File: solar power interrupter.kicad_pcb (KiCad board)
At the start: 2 copper layers, 25.4 x 33 mm, 18 parts, among them J1 USB_C_Receptacle_USB2.0, J2 Screw_Terminal_01x04, Q1 BSS138, Q2 BSS138, Q3 BSS84

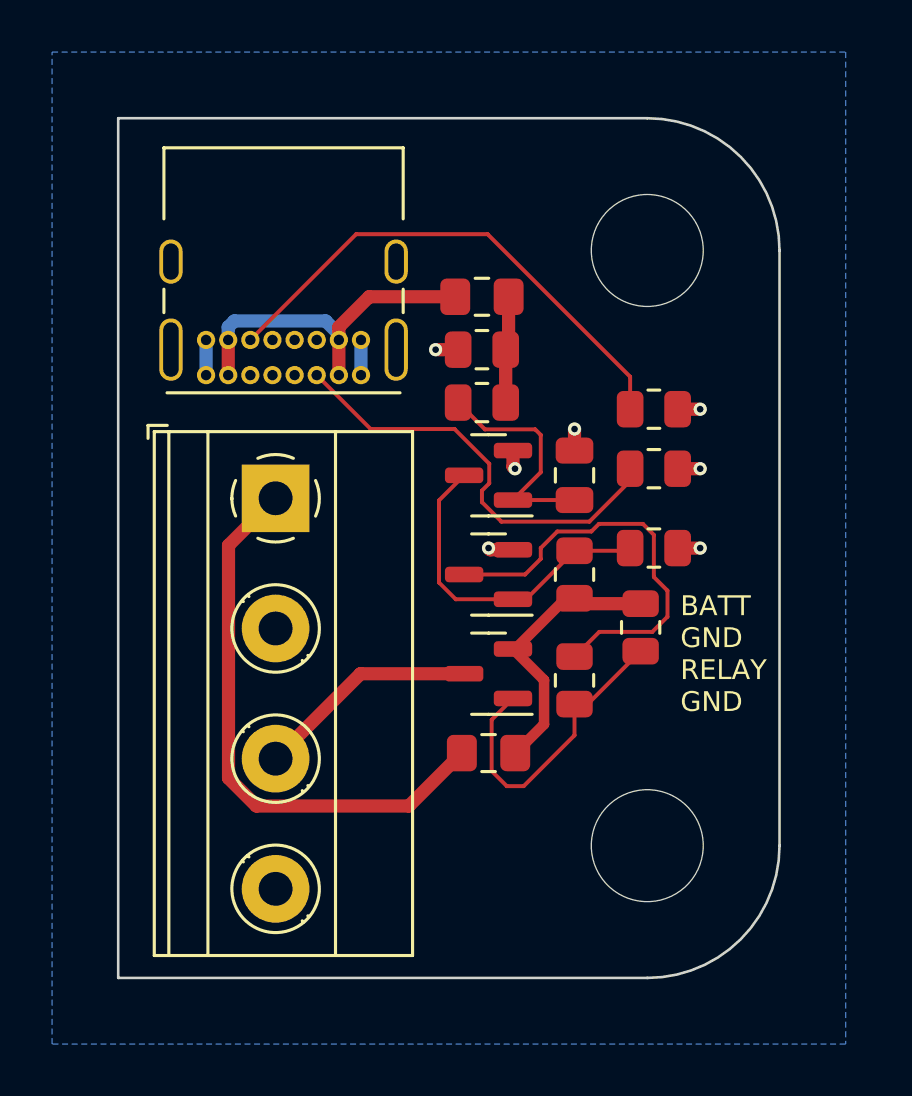
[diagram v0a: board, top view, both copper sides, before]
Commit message: added protection to battery connection, changed pins on connector for safety, added zener diodes to limit Vgs, added protection for relay drive pin
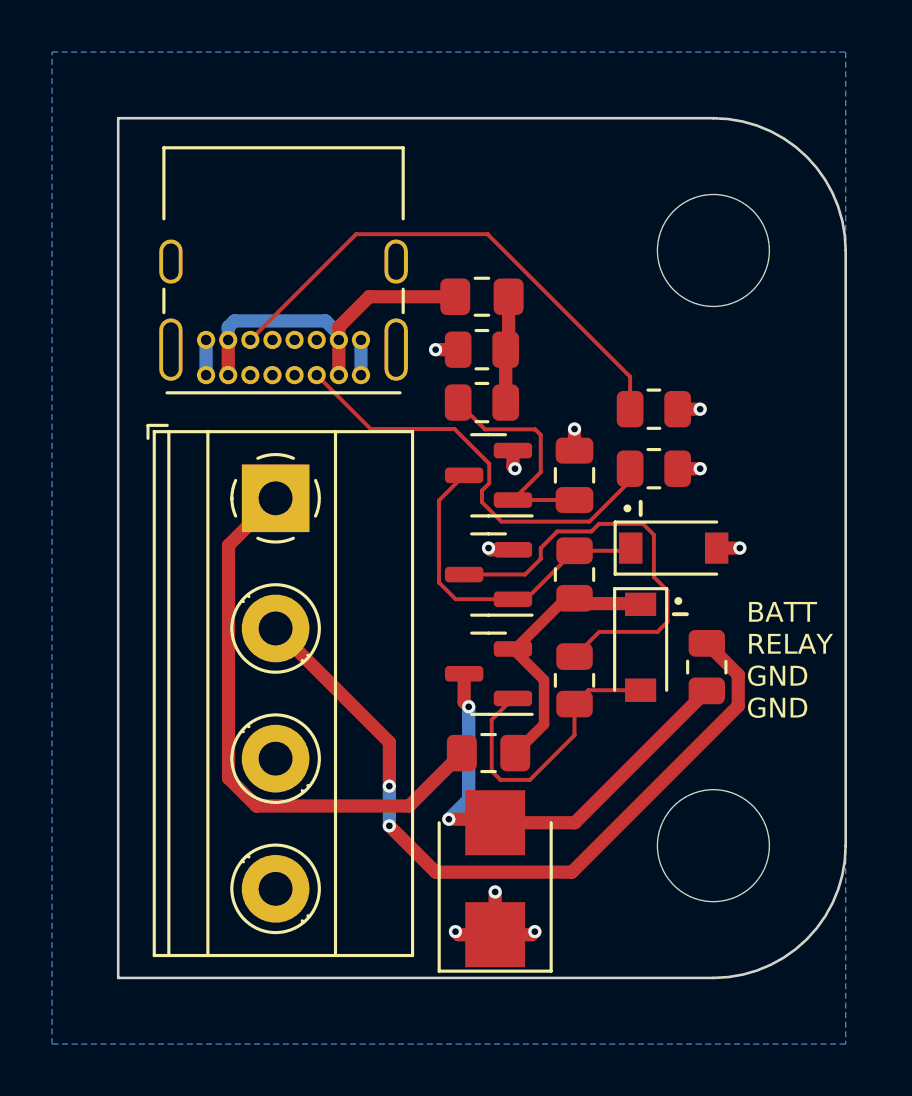
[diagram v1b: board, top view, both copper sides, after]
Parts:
- removed R8: 40K, Resistor_SMD:R_0805_2012Metric
- added D1: D_Zener, Diode_SMD:D_SOD-123, F.Cu at (54.4, 166.4)
- added D2: D_Zener, Diode_SMD:D_SOD-123, F.Cu at (53.1, 170.2)
- added D3: D_TVS, Diode_SMD:D_SMB, F.Cu at (47.5, 179.1)
- F1: value Fuse -> USB Fuse
- F2: value Fuse -> Batt Fuse
- R4, R5: value 60K -> 56k
- R6: value 6K -> 6.2K
- R7: value 40k -> 2.7K
- moved R7 5.00 mm to (55.6, 170.9), turned to 90 degrees
- moved H1 2.54 mm to (55.9, 154.9)
- moved H2 2.54 mm to (55.9, 177.8)
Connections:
- J2 pad 2: GND -> /RELAY
- J2 pad 3: /RELAY -> GND
- Q1 pad 3: Net-(Q1-Pad3) -> Net-(D1-Pad1)
- Q2 pad 1: Net-(Q1-Pad3) -> Net-(D1-Pad1)
- Q3 pad 3: /RELAY -> /RELAY_UNPROTECTED
- R4 pad 2: Net-(Q1-Pad3) -> Net-(D1-Pad1)
- R7 pad 1: Net-(Q1-Pad3) -> /RELAY_UNPROTECTED
- R7 pad 2: GND -> /RELAY
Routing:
- net /RELAY: track 8.59 -> 29.1 mm, vias 0 -> 2
- net /RELAY_UNPROTECTED: track 0.00 -> 18.0 mm, vias 0 -> 2
- net Net-(Q1-Pad3): track 12.3 -> 0.00 mm
- net Net-(D1-Pad1): track 0.00 -> 12.3 mm
- net GND: track 8.68 -> 13.5 mm, vias 7 -> 10
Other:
- board size 25.4 x 33 mm -> 27.9 x 33 mm
- board text added: "BATT RELAY GND GND"
- board text removed: "BATT GND RELAY GND"

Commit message: updated simulation added needed pullup resistor, note this wasn't included in the PCB that I ordered. added images to readme.
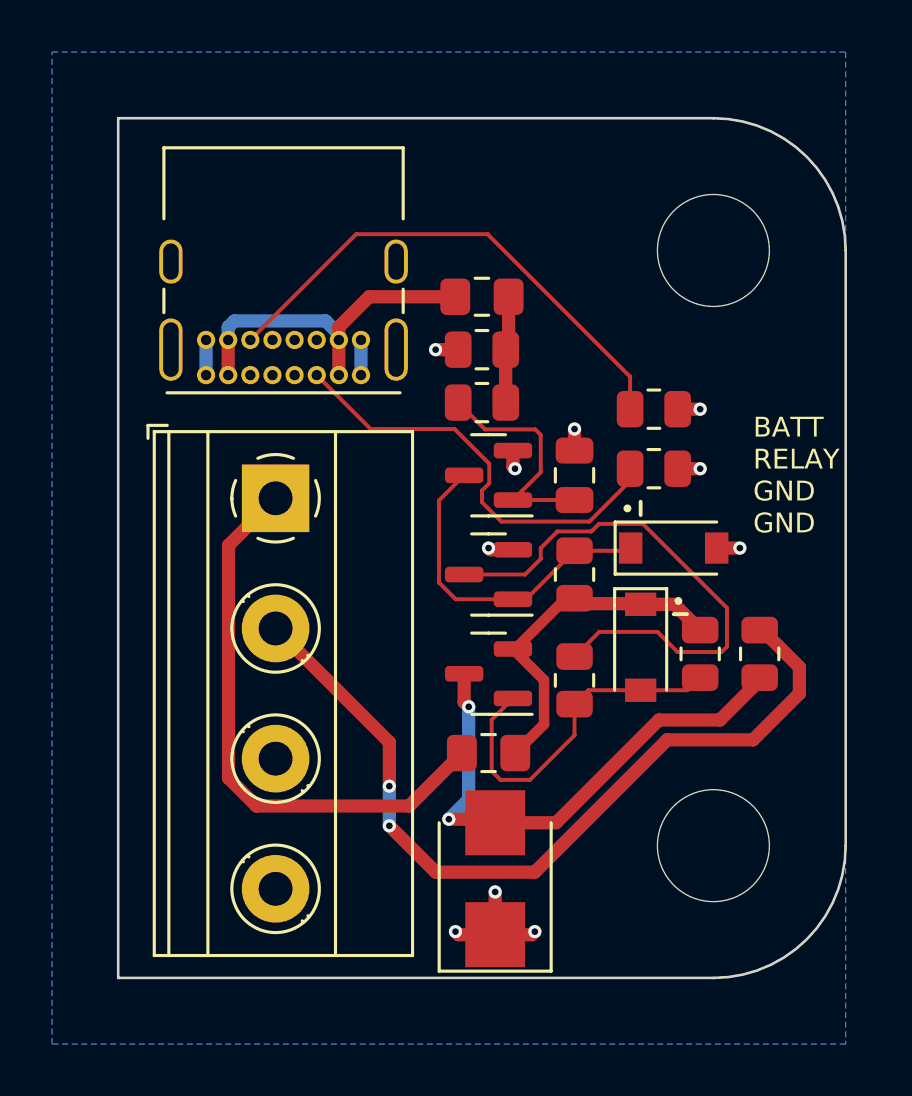
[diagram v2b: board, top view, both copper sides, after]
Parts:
- added R8: 56k, Resistor_SMD:R_0805_2012Metric, F.Cu at (55.4, 170.4)
- R5: value 56k -> 10k
- moved R7 2.09 mm to (57.7, 170.4)
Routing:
- net Net-(Q2-Pad3): track 16.2 -> 20.6 mm
- net +BATT: track 10.0 -> 12.7 mm
- net /RELAY: track 29.1 -> 31.7 mm
- net Net-(D2-Pad2): track 11.1 -> 13.6 mm
- net /RELAY_UNPROTECTED: track 18.0 -> 20.2 mm
